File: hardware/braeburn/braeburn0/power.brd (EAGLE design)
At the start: 100 x 80 mm, 48 parts, among them IC1 7812TV, IC2 7805TV, IC3 7805TV, IC4 ATMEGA48/88/168-AU, IC5 LM741D, IC6 MAX481CSA, IC7 LM741D

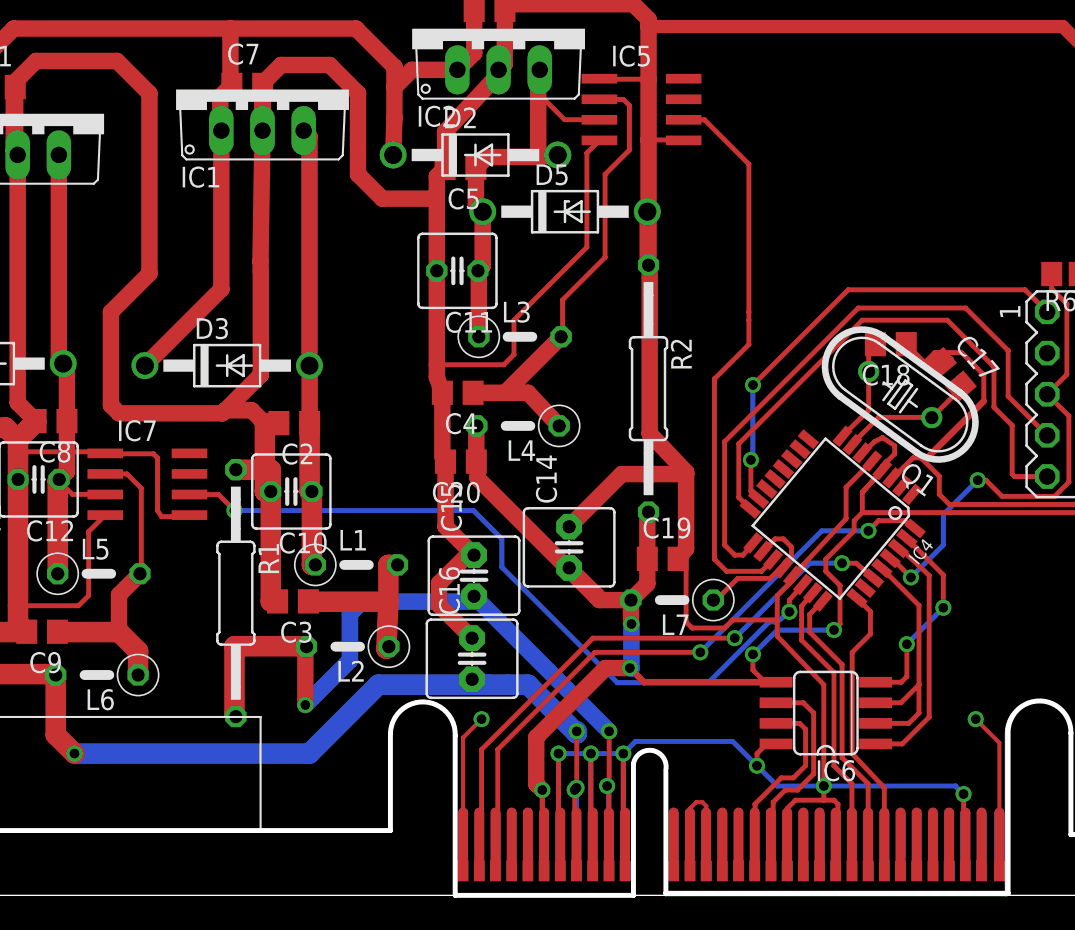
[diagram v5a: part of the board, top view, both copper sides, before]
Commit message: minor improvements, thicker power lines
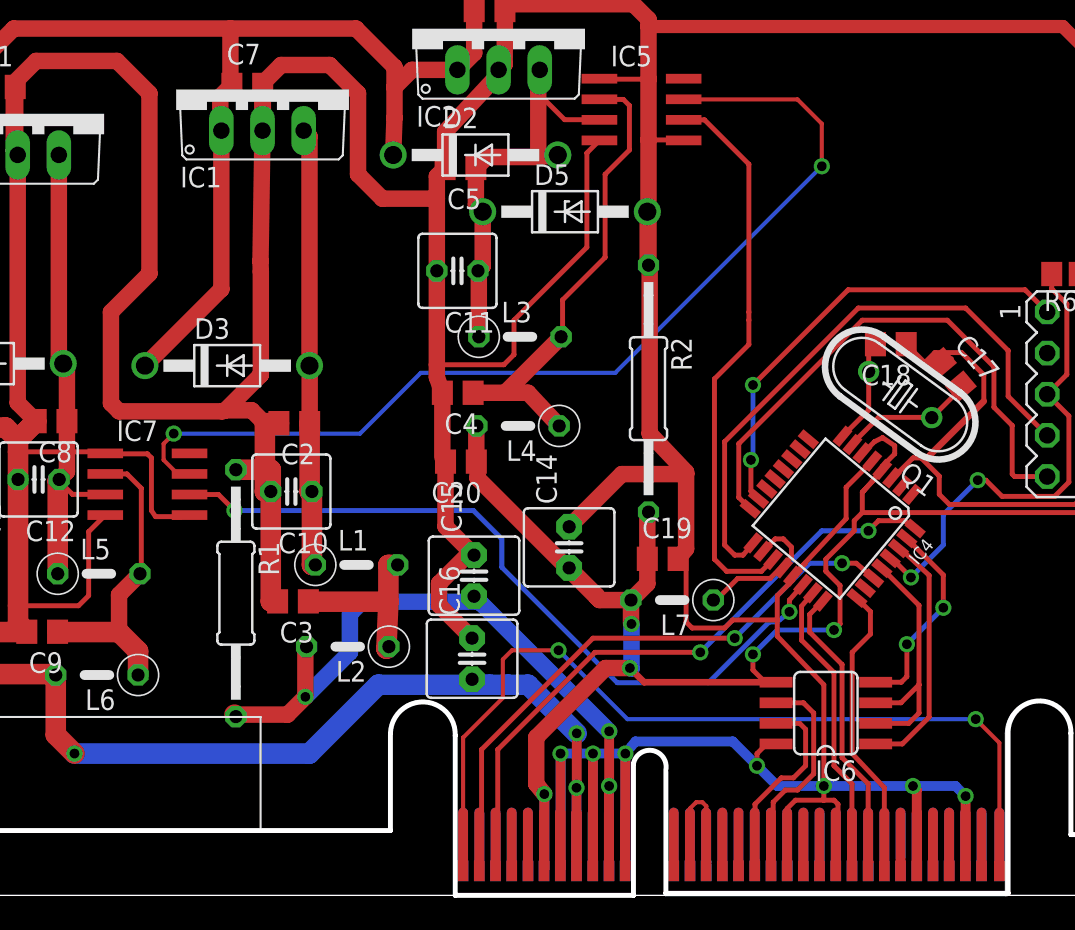
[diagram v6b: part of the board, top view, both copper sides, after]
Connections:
- removed net N$3: IC7.7
- removed net N$4: IC7.8
- removed net N$6: IC5.7
- removed net N$7: IC5.8
- new net V+: IC5.7, IC7.7
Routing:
- net V+: track 0.00 -> 62.5 mm, vias 0 -> 2
- net N$34: track 20.2 -> 55.5 mm
- net +12V: track 53.8 -> 48.8 mm
- net GND: track 529.6 -> 534.4 mm, vias 6 -> 7
- net +5V: track 61.7 -> 61.5 mm, vias 4 -> 3

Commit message: .
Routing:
- net 5VMETER: track 46.6 -> 50.1 mm
- net GND: track 534.4 -> 535.6 mm

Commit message: slight update
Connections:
- removed net V+: IC5.7, IC7.7
- net +3V3: now also IC5.7, IC7.7
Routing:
- net V+: track 62.5 -> 0.00 mm, vias 2 -> 0
- net +3V3: track 118.6 -> 180.8 mm, vias 7 -> 11
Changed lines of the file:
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@@
 <wire x1="68.875" y1="16.75" x2="68.5" y2="16.375" width="0.3048" layer="1"/>
 <via x="68.5" y="16.375" extent="1-16" drill="0.6"/>
-<wire x1="68.5" y1="16.375" x2="65" y2="16.375" width="0.3048" layer="16"/>
-<wire x1="65" y1="16.375" x2="63.5" y2="14.875" width="0.3048" layer="16"/>
-<via x="63.5" y="14.875" extent="1-16" drill="0.6"/>
-<wire x1="63.5" y1="14.875" x2="63.5" y2="13.905" width="0.3048" layer="1"/>
-<wire x1="63.5" y1="13.905" x2="64.25" y2="13.155" width="0.3048" layer="1"/>
+<wire x1="68.5" y1="16.375" x2="65.4375" y2="16.375" width="0.3048" layer="16"/>
+<wire x1="65.4375" y1="16.375" x2="63.6875" y2="14.625" width="0.3048" layer="16"/>
+<via x="63.6875" y="14.625" extent="1-16" drill="0.6"/>
+<wire x1="63.6875" y1="14.625" x2="63.6875" y2="13.7175" width="0.3048" layer="1"/>
+<wire x1="63.6875" y1="13.7175" x2="64.25" y2="13.155" width="0.3048" layer="1"/>
 <wire x1="64.25" y1="13.155" x2="56.78" y2="13.155" width="0.4064" layer="1"/>
 <wire x1="56.78" y1="13.155" x2="55.905" y2="14.03" width="0.4064" layer="1"/>
@@
 <wire x1="55.975" y1="18.225" x2="54.025" y2="18.225" width="1.016" layer="1"/>
 <wire x1="54.025" y1="18.225" x2="53.875" y2="18.375" width="1.016" layer="1"/>
-<wire x1="53.875" y1="18.375" x2="46.5" y2="25.75" width="1.016" layer="1"/>
+<wire x1="53.875" y1="18.375" x2="47.75" y2="24.5" width="1.016" layer="1"/>
+<wire x1="47.75" y1="24.5" x2="47.625" y2="24.625" width="1.016" layer="1"/>
+<wire x1="47.625" y1="24.625" x2="46.5" y2="25.75" width="1.016" layer="1"/>
 <wire x1="46.5" y1="25.75" x2="46.5" y2="26.695" width="1.016" layer="1"/>
 <wire x1="46.5" y1="26.695" x2="46.425" y2="26.77" width="1.016" layer="1"/>
@@
 <wire x1="86.375" y1="33.875" x2="86.335" y2="33.875" width="0.3048" layer="1"/>
 <wire x1="86.335" y1="33.875" x2="84.2" y2="36.01" width="0.3048" layer="1"/>
+<contactref element="IC7" pad="7"/>
+<contactref element="IC5" pad="7"/>
+<wire x1="28.725" y1="26.01" x2="27.5525" y2="26.01" width="0.4064" layer="1"/>
+<wire x1="27.5525" y1="26.01" x2="26.9375" y2="26.625" width="0.4064" layer="1"/>
+<wire x1="26.9375" y1="26.625" x2="26.9375" y2="28" width="0.4064" layer="1"/>
+<wire x1="26.9375" y1="28" x2="27.1875" y2="28.25" width="0.4064" layer="1"/>
+<wire x1="27.1875" y1="28.25" x2="30.9375" y2="28.25" width="0.4064" layer="1"/>
+<wire x1="30.9375" y1="28.25" x2="31.0625" y2="28.375" width="0.4064" layer="1"/>
+<via x="31.0625" y="28.375" extent="1-16" drill="0.6" shape="square"/>
+<wire x1="31.0625" y1="28.375" x2="38.625" y2="28.375" width="0.4064" layer="16"/>
+<wire x1="38.625" y1="28.375" x2="41.6875" y2="25.3125" width="0.4064" layer="16"/>
+<wire x1="41.6875" y1="25.3125" x2="44.625" y2="25.3125" width="0.4064" layer="16"/>
+<wire x1="44.625" y1="25.3125" x2="46" y2="23.9375" width="0.4064" layer="16"/>
+<via x="46" y="23.9375" extent="1-16" drill="0.6"/>
+<wire x1="46" y1="23.9375" x2="46.9375" y2="23.9375" width="0.4064" layer="1"/>
+<wire x1="46.9375" y1="23.9375" x2="47.625" y2="24.625" width="0.4064" layer="1"/>
+<wire x1="59.225" y1="49.135" x2="61.0525" y2="49.135" width="0.4064" layer="1"/>
+<wire x1="61.0525" y1="49.135" x2="64.5" y2="45.6875" width="0.4064" layer="1"/>
+<wire x1="64.5" y1="45.6875" x2="64.5" y2="39.375" width="0.4064" layer="1"/>
+<wire x1="64.5" y1="39.375" x2="64.4375" y2="39.3125" width="0.4064" layer="1"/>
+<via x="64.4375" y="39.3125" extent="1-16" drill="0.6" shape="square"/>
+<wire x1="64.4375" y1="39.3125" x2="64.4375" y2="38.9375" width="0.4064" layer="16"/>
+<wire x1="64.4375" y1="38.9375" x2="54" y2="28.5" width="0.4064" layer="16"/>
+<wire x1="54" y1="28.5" x2="54" y2="28.3125" width="0.4064" layer="16"/>
+<wire x1="54" y1="28.3125" x2="50.8125" y2="25.125" width="0.4064" layer="16"/>
+<via x="50.8125" y="25.125" extent="1-16" drill="0.6"/>
+<wire x1="50.8125" y1="25.125" x2="48.375" y2="25.125" width="0.4064" layer="1"/>
+<wire x1="48.375" y1="25.125" x2="47.75" y2="24.5" width="0.4064" layer="1"/>
 <wire x1="84.21" y1="36" x2="84.25" y2="36" width="0" layer="19" extent="1-1"/>
 <wire x1="84.25" y1="35.375" x2="84.25" y2="35.75" width="0" layer="19" extent="1-1"/>
@@
 <via x="65.75" y="17.5" extent="1-16" drill="0.6"/>
 <wire x1="65.75" y1="17.5" x2="65" y2="16.875" width="0.3048" layer="16"/>
-<wire x1="65" y1="16.875" x2="64.5" y2="16.875" width="0.3048" layer="16"/>
-<wire x1="64.5" y1="16.875" x2="60.75" y2="13.125" width="0.3048" layer="16"/>
-<wire x1="60.75" y1="13.125" x2="55.125" y2="13.125" width="0.3048" layer="16"/>
+<wire x1="65" y1="16.875" x2="64.6875" y2="16.875" width="0.3048" layer="16"/>
+<wire x1="64.6875" y1="16.875" x2="60.9375" y2="13.125" width="0.3048" layer="16"/>
+<wire x1="60.9375" y1="13.125" x2="55.125" y2="13.125" width="0.3048" layer="16"/>
 <wire x1="55.125" y1="13.125" x2="48" y2="20.25" width="0.3048" layer="16"/>
 <wire x1="48" y1="20.25" x2="48" y2="22" width="0.3048" layer="16"/>
@@
 <wire x1="24.375" y1="18.555" x2="24.375" y2="16.25" width="0.8128" layer="1"/>
 </signal>
-<signal name="V+">
-<contactref element="IC7" pad="7"/>
-<contactref element="IC5" pad="7"/>
-<wire x1="28.725" y1="26.01" x2="27.99" y2="26.01" width="0.254" layer="1"/>
-<wire x1="27.99" y1="26.01" x2="27.125" y2="26.875" width="0.254" layer="1"/>
-<wire x1="27.125" y1="26.875" x2="27.125" y2="27.875" width="0.254" layer="1"/>
-<wire x1="27.125" y1="27.875" x2="27.75" y2="28.5" width="0.254" layer="1"/>
-<via x="27.75" y="28.5" extent="1-16" drill="0.6"/>
-<wire x1="27.75" y1="28.5" x2="39.25" y2="28.5" width="0.254" layer="16"/>
-<wire x1="39.25" y1="28.5" x2="43" y2="32.25" width="0.254" layer="16"/>
-<wire x1="43" y1="32.25" x2="55" y2="32.25" width="0.254" layer="16"/>
-<wire x1="55" y1="32.25" x2="67.75" y2="45" width="0.254" layer="16"/>
-<via x="67.75" y="45" extent="1-16" drill="0.6" shape="square"/>
-<wire x1="67.75" y1="45" x2="67.75" y2="47.625" width="0.254" layer="1"/>
-<wire x1="67.75" y1="47.625" x2="66.25" y2="49.125" width="0.254" layer="1"/>
-<wire x1="66.25" y1="49.125" x2="59.235" y2="49.125" width="0.254" layer="1"/>
-<wire x1="59.235" y1="49.125" x2="59.225" y2="49.135" width="0.254" layer="1"/>
-</signal>
 </signals>
